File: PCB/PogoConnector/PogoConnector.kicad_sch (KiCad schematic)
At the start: 7 parts, among them J1 PogoPinPad, J2 Conn_01x06, J3 PogoPinPad, J4 PogoPinPad, U1 PogoPin, U2 PogoPin, U3 PogoPin

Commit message: Update PCB
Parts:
- J2: footprint Connector_PinHeader_2.54mm:PinHeader_1x06_P2.54mm_Vertical -> CustomFootprints:Connector_PinHeader_2.54mm_Vertical; now left out of the parts list
- U1, U2, U3: LCSC C2826552 -> C2988082
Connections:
- net +5V: now also J2.1 (Pin_1), J2.6 (Pin_6), J4.1 (Pin_1), U1.1; no longer J2.2 (Pin_2), J2.5 (Pin_5), J3.1 (Pin_1), U2.1
- net Data1: now also J2.2 (Pin_2), U2.1; no longer J1.1 (Pin_1), J2.4 (Pin_4)
- net Data2: now also J2.5 (Pin_5), J3.1 (Pin_1); no longer J2.3 (Pin_3), U3.1
- net GND: now also J1.1 (Pin_1), J2.3 (Pin_3), J2.4 (Pin_4), U3.1; no longer J2.1 (Pin_1), J2.6 (Pin_6), J4.1 (Pin_1), U1.1

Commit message: Add hall sensor shield
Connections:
- net +5V: no longer J2.6 (Pin_6), J4.1 (Pin_1)
- net GND: no longer J1.1 (Pin_1), J2.4 (Pin_4)
- new net +5V2: J2.6 (Pin_6), J4.1 (Pin_1)
- new net GND2: J1.1 (Pin_1), J2.4 (Pin_4)
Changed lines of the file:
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@@
 	(paper "A4")
+	(junction
+		(at 128.27 91.44)
+		(diameter 0)
+		(color 0 0 0 0)
+	)
 	(junction
 		(at 135.89 86.36)
@@
 	)
 	(junction
-		(at 128.27 93.98)
+		(at 138.43 99.06)
 		(diameter 0)
 		(color 0 0 0 0)
 	)
 	(junction
-		(at 135.89 99.06)
-		(diameter 0)
-		(color 0 0 0 0)
-	)
-	(junction
-		(at 140.97 104.14)
+		(at 125.73 93.98)
 		(diameter 0)
 		(color 0 0 0 0)
@@
 	)
 	(junction
-		(at 128.27 91.44)
-		(diameter 0)
-		(color 0 0 0 0)
-	)
-	(junction
 		(at 133.35 96.52)
 		(diameter 0)
@@
 	(wire
 		(pts
-			(xy 140.97 99.06) (xy 140.97 104.14)
-		)
-		(stroke
-			(width 0)
-			(type default)
-		)
-	)
-	(wire
-		(pts
 			(xy 135.89 86.36) (xy 140.97 86.36)
 		)
@@
 	(wire
 		(pts
-			(xy 135.89 86.36) (xy 135.89 99.06)
-		)
-		(stroke
-			(width 0)
-			(type default)
-		)
-	)
-	(wire
-		(pts
 			(xy 133.35 107.95) (xy 133.35 96.52)
 		)
@@
 	(wire
 		(pts
-			(xy 123.19 93.98) (xy 128.27 93.98)
+			(xy 123.19 93.98) (xy 125.73 93.98)
 		)
 		(stroke
@@
 	(wire
 		(pts
-			(xy 128.27 93.98) (xy 128.27 91.44)
-		)
-		(stroke
-			(width 0)
-			(type default)
-		)
-	)
-	(wire
-		(pts
-			(xy 135.89 99.06) (xy 135.89 111.76)
+			(xy 128.27 93.98) (xy 140.97 93.98)
+		)
+		(stroke
+			(width 0)
+			(type default)
+		)
+	)
+	(wire
+		(pts
+			(xy 128.27 91.44) (xy 128.27 93.98)
+		)
+		(stroke
+			(width 0)
+			(type default)
+		)
+	)
+	(wire
+		(pts
+			(xy 138.43 99.06) (xy 138.43 111.76)
+		)
+		(stroke
+			(width 0)
+			(type default)
+		)
+	)
+	(wire
+		(pts
+			(xy 138.43 83.82) (xy 138.43 99.06)
 		)
 		(stroke
@@
 	(wire
 		(pts
+			(xy 140.97 93.98) (xy 140.97 99.06)
+		)
+		(stroke
+			(width 0)
+			(type default)
+		)
+	)
+	(wire
+		(pts
 			(xy 133.35 96.52) (xy 123.19 96.52)
 		)
@@
 	(wire
 		(pts
-			(xy 135.89 111.76) (xy 140.97 111.76)
-		)
-		(stroke
-			(width 0)
-			(type default)
-		)
-	)
-	(wire
-		(pts
-			(xy 128.27 104.14) (xy 128.27 93.98)
+			(xy 138.43 111.76) (xy 140.97 111.76)
+		)
+		(stroke
+			(width 0)
+			(type default)
+		)
+	)
+	(wire
+		(pts
+			(xy 125.73 104.14) (xy 125.73 93.98)
 		)
 		(stroke
@@
 	(wire
 		(pts
-			(xy 140.97 104.14) (xy 128.27 104.14)
+			(xy 140.97 104.14) (xy 125.73 104.14)
 		)
 		(stroke
@@
 	(wire
 		(pts
+			(xy 125.73 83.82) (xy 125.73 93.98)
+		)
+		(stroke
+			(width 0)
+			(type default)
+		)
+	)
+	(wire
+		(pts
 			(xy 128.27 91.44) (xy 123.19 91.44)
 		)
@@
 	(wire
 		(pts
-			(xy 135.89 99.06) (xy 123.19 99.06)
+			(xy 138.43 99.06) (xy 123.19 99.06)
 		)
 		(stroke
@@
 				(path "/22410f48-dad6-45f0-8cac-d86f69190735"
 					(reference "J3")
+					(unit 1)
+				)
+			)
+		)
+	)
+	(symbol
+		(lib_id "power:GND2")
+		(at 125.73 83.82 180)
+		(unit 1)
+		(exclude_from_sim no)
+		(in_bom yes)
+		(on_board yes)
+		(dnp no)
+		(fields_autoplaced yes)
+		(property "Reference" "#PWR3"
+			(at 125.73 77.47 0)
+			(effects
+				(font
+					(size 1.27 1.27)
+				)
+				(hide yes)
+			)
+		)
+		(property "Value" "GND2"
+			(at 125.73 78.74 0)
+			(effects
+				(font
+					(size 1.27 1.27)
+				)
+			)
+		)
+		(property "Footprint" ""
+			(at 125.73 83.82 0)
+			(effects
+				(font
+					(size 1.27 1.27)
+				)
+				(hide yes)
+			)
+		)
+		(property "Datasheet" ""
+			(at 125.73 83.82 0)
+			(effects
+				(font
+					(size 1.27 1.27)
+				)
+				(hide yes)
+			)
+		)
+		(property "Description" "Power symbol creates a global label with name \"GND2\" , ground"
+			(at 125.73 83.82 0)
+			(effects
+				(font
+					(size 1.27 1.27)
+				)
+				(hide yes)
+			)
+		)
+		(pin "1"
+		)
+		(instances
+			(project ""
+				(path "/22410f48-dad6-45f0-8cac-d86f69190735"
+					(reference "#PWR3")
 					(unit 1)
 				)
@@
 					(unit 1)
 				)
+			)
+		)
+	)
+	(symbol
+		(lib_id "power:+5V")
+		(at 138.43 83.82 0)
+		(mirror y)
+		(unit 1)
+		(exclude_from_sim no)
+		(in_bom yes)
+		(on_board yes)
+		(dnp no)
+		(property "Reference" "#PWR4"
+			(at 138.43 87.63 0)
+			(effects
+				(font
+					(size 1.27 1.27)
+				)
+				(hide yes)
+			)
+		)
+		(property "Value" "+5V2"
+			(at 138.43 78.74 0)
+			(effects
+				(font
+					(size 1.27 1.27)
+				)
+			)
+		)
+		(property "Footprint" ""
+			(at 138.43 83.82 0)
+			(effects
+				(font
+					(size 1.27 1.27)
+				)
+				(hide yes)
+			)
+		)
+		(property "Datasheet" ""
+			(at 138.43 83.82 0)
+			(effects
+				(font
+					(size 1.27 1.27)
+				)
+				(hide yes)
+			)
+		)
+		(property "Description" "Power symbol creates a global label with name \"+5V\""
+			(at 138.43 83.82 0)
+			(effects
+				(font
+					(size 1.27 1.27)
+				)
+				(hide yes)
+			)
+		)
+		(pin "1"
+		)
+		(instances
+			(project "PogoConnector"
+				(path "/22410f48-dad6-45f0-8cac-d86f69190735"
+					(reference "#PWR4")
+					(unit 1)
+				)

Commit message: Add power supply (wip) and update panel
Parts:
- J1, J3, J4: now left out of the parts list
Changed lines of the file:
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@@
 		(unit 1)
 		(exclude_from_sim no)
-		(in_bom yes)
+		(in_bom no)
 		(on_board yes)
 		(dnp no)
@@
 		(unit 1)
 		(exclude_from_sim no)
-		(in_bom yes)
+		(in_bom no)
 		(on_board yes)
 		(dnp no)
@@
 		(unit 1)
 		(exclude_from_sim no)
-		(in_bom yes)
-		(on_board yes)
-		(dnp no)
+		(in_bom no)
+		(on_board yes)
+		(dnp no)

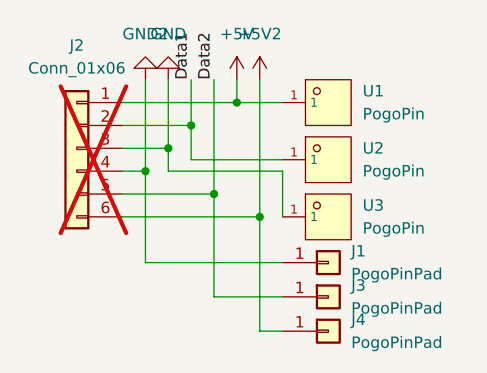
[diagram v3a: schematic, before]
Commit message: Finish module, power supply and connector design, panel is wip
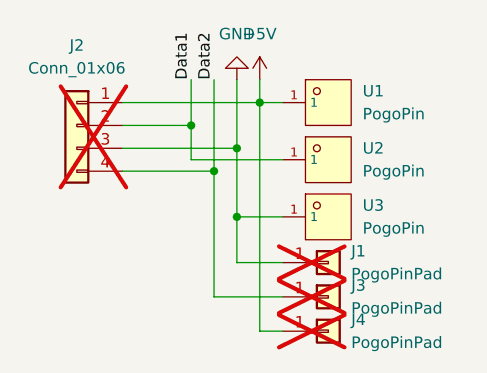
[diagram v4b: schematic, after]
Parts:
- J1, J3, J4: now not fitted
- J2: footprint CustomFootprints:Connector_PinHeader_2.54mm_Vertical -> CustomFootprints:01x04_PinPads; symbol Connector_Generic:Conn_01x06 -> Connector_Generic:Conn_01x04; now in the parts list
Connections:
- net +5V: now also J4.1 (Pin_1)
- net Data2: now also J2.4 (Pin_4); no longer J2.5 (Pin_5)
- net GND: now also J1.1 (Pin_1)
- removed net +5V2: J2.6 (Pin_6), J4.1 (Pin_1)
- removed net GND2: J1.1 (Pin_1), J2.4 (Pin_4)

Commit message: Finish panel script
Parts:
- added J5: Conn_01x06, CustomFootprints:01x04_PinPads_Single, symbol Connector_Generic:Conn_01x04
- J2: footprint CustomFootprints:01x04_PinPads -> CustomFootprints:01x04_PinPads_Single; now left out of the parts list
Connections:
- net +5V: now also J5.1 (Pin_1), J5.2 (Pin_2), J5.3 (Pin_3), J5.4 (Pin_4)
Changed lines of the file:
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@@
 	(paper "A4")
 	(junction
+		(at 123.19 107.95)
+		(diameter 0)
+		(color 0 0 0 0)
+	)
+	(junction
 		(at 138.43 86.36)
 		(diameter 0)
@@
 		(color 0 0 0 0)
 	)
+	(junction
+		(at 123.19 105.41)
+		(diameter 0)
+		(color 0 0 0 0)
+	)
+	(junction
+		(at 123.19 102.87)
+		(diameter 0)
+		(color 0 0 0 0)
+	)
 	(wire
 		(pts
@@
 	(wire
 		(pts
+			(xy 123.19 105.41) (xy 123.19 107.95)
+		)
+		(stroke
+			(width 0)
+			(type default)
+		)
+	)
+	(wire
+		(pts
 			(xy 138.43 86.36) (xy 140.97 86.36)
 		)
@@
 	(wire
 		(pts
+			(xy 123.19 102.87) (xy 123.19 105.41)
+		)
+		(stroke
+			(width 0)
+			(type default)
+		)
+	)
+	(wire
+		(pts
 			(xy 140.97 107.95) (xy 133.35 107.95)
+		)
+		(stroke
+			(width 0)
+			(type default)
+		)
+	)
+	(wire
+		(pts
+			(xy 123.19 107.95) (xy 123.19 110.49)
 		)
 		(stroke
@@
 			)
 			(justify left bottom)
+		)
+	)
+	(symbol
+		(lib_id "Connector_Generic:Conn_01x04")
+		(at 118.11 105.41 0)
+		(mirror y)
+		(unit 1)
+		(exclude_from_sim no)
+		(in_bom no)
+		(on_board yes)
+		(dnp yes)
+		(fields_autoplaced yes)
+		(property "Reference" "J5"
+			(at 118.11 96.52 0)
+			(effects
+				(font
+					(size 1.27 1.27)
+				)
+			)
+		)
+		(property "Value" "Conn_01x06"
+			(at 118.11 99.06 0)
+			(effects
+				(font
+					(size 1.27 1.27)
+				)
+			)
+		)
+		(property "Footprint" "CustomFootprints:01x04_PinPads_Single"
+			(at 118.11 105.41 0)
+			(effects
+				(font
+					(size 1.27 1.27)
+				)
+				(hide yes)
+			)
+		)
+		(property "Datasheet" "~"
+			(at 118.11 105.41 0)
+			(effects
+				(font
+					(size 1.27 1.27)
+				)
+				(hide yes)
+			)
+		)
+		(property "Description" "Generic connector, single row, 01x04, script generated (kicad-library-utils/schlib/autogen/connector/)"
+			(at 118.11 105.41 0)
+			(effects
+				(font
+					(size 1.27 1.27)
+				)
+				(hide yes)
+			)
+		)
+		(pin "3"
+		)
+		(pin "1"
+		)
+		(pin "2"
+		)
+		(pin "4"
+		)
+		(instances
+			(project "PogoConnector"
+				(path "/22410f48-dad6-45f0-8cac-d86f69190735"
+					(reference "J5")
+					(unit 1)
+				)
+			)
 		)
 	)
@@
 	)
 	(symbol
+		(lib_id "power:+5V")
+		(at 123.19 102.87 0)
+		(mirror y)
+		(unit 1)
+		(exclude_from_sim no)
+		(in_bom yes)
+		(on_board yes)
+		(dnp no)
+		(property "Reference" "#PWR3"
+			(at 123.19 106.68 0)
+			(effects
+				(font
+					(size 1.27 1.27)
+				)
+				(hide yes)
+			)
+		)
+		(property "Value" "+5V"
+			(at 123.19 97.79 0)
+			(effects
+				(font
+					(size 1.27 1.27)
+				)
+			)
+		)
+		(property "Footprint" ""
+			(at 123.19 102.87 0)
+			(effects
+				(font
+					(size 1.27 1.27)
+				)
+				(hide yes)
+			)
+		)
+		(property "Datasheet" ""
+			(at 123.19 102.87 0)
+			(effects
+				(font
+					(size 1.27 1.27)
+				)
+				(hide yes)
+			)
+		)
+		(property "Description" "Power symbol creates a global label with name \"+5V\""
+			(at 123.19 102.87 0)
+			(effects
+				(font
+					(size 1.27 1.27)
+				)
+				(hide yes)
+			)
+		)
+		(pin "1"
+		)
+		(instances
+			(project "PogoConnector"
+				(path "/22410f48-dad6-45f0-8cac-d86f69190735"
+					(reference "#PWR3")
+					(unit 1)
+				)
+			)
+		)
+	)
+	(symbol
 		(lib_id "Connector_Generic:Conn_01x01")
 		(at 146.05 107.95 0)
@@
 		(unit 1)
 		(exclude_from_sim no)
-		(in_bom yes)
+		(in_bom no)
 		(on_board yes)
 		(dnp yes)
@@
 			)
 		)
-		(property "Footprint" "CustomFootprints:01x04_PinPads"
+		(property "Footprint" "CustomFootprints:01x04_PinPads_Single"
 			(at 118.11 88.9 0)
 			(effects
